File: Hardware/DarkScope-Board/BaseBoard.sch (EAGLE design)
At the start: 85 parts, among them IC1 7805DT, IC2 REG1117, IC3 7905, J1 DCJ0202, Q1 8MHz, T2 9014, U1 STM32F103CBT6, X1 TSW-102-07-G-S, X2 TSW-102-07-G-S, X3 MINI-USB-32005-301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

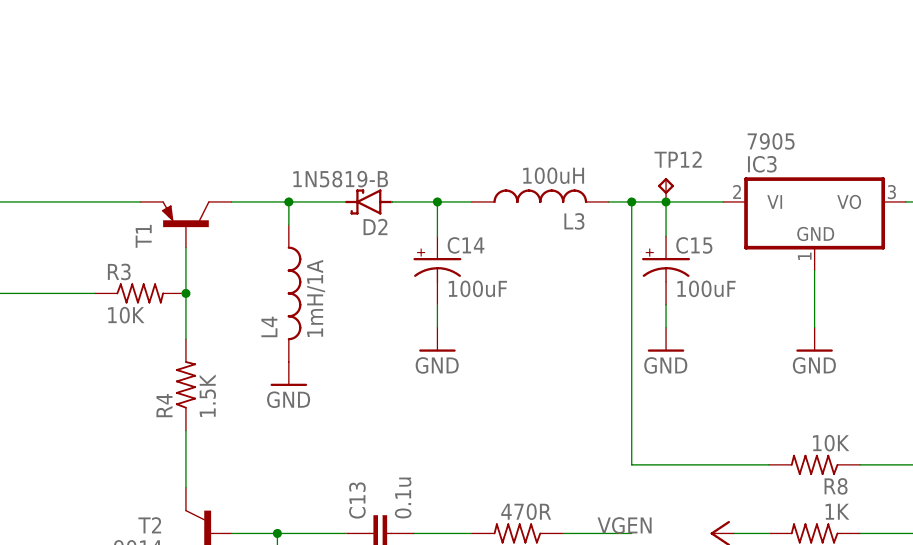
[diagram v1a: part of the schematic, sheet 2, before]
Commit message: Fixed BaseBoard Bugs
1. Ground Plane Not connected Properly
2. C14,C15 Reversed.
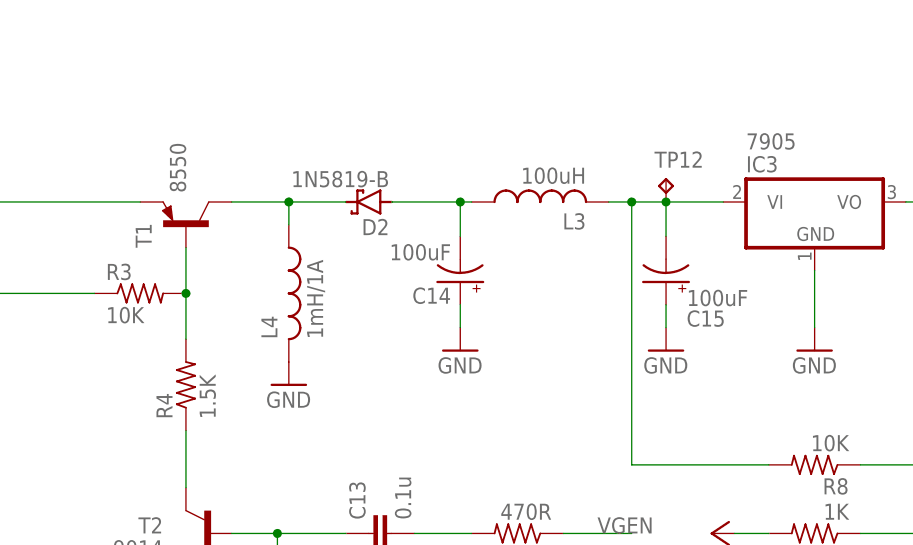
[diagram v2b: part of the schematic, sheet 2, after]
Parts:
- T1: value (none) -> 8550
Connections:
- net GND: now also C14.+, C15.+; no longer C14.-, C15.-
- net N$12: now also C14.-; no longer C14.+
- net N$13: now also C15.-; no longer C15.+
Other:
- moved on the sheet: C14, C15
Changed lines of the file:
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@@
 <setting verticaltext="up"/>
 </settings>
-<grid distance="0.1" unitdist="inch" unit="inch" style="lines" multiple="1" display="no" altdistance="0.01" altunitdist="inch" altunit="inch"/>
+<grid distance="0.01" unitdist="inch" unit="inch" style="lines" multiple="1" display="no" altdistance="0.01" altunitdist="inch" altunit="inch"/>
 <layers>
 <layer number="1" name="Top" color="4" fill="1" visible="no" active="no"/>
@@
 <part name="P+2" library="supply1" library_urn="urn:adsk.eagle:library:371" deviceset="+12V" device=""/>
 <part name="P+3" library="supply1" library_urn="urn:adsk.eagle:library:371" deviceset="+12V" device=""/>
-<part name="T1" library="transistor" library_urn="urn:adsk.eagle:library:402" deviceset="*-PNP-" device="TO92" package3d_urn="urn:adsk.eagle:package:28523/2"/>
+<part name="T1" library="transistor" library_urn="urn:adsk.eagle:library:402" deviceset="*-PNP-" device="TO92" package3d_urn="urn:adsk.eagle:package:28523/2" value="8550"/>
 <part name="R3" library="rcl" library_urn="urn:adsk.eagle:library:334" deviceset="R-US_" device="R0805" package3d_urn="urn:adsk.eagle:package:23553/2" value="10K"/>
 <part name="R4" library="rcl" library_urn="urn:adsk.eagle:library:334" deviceset="R-US_" device="R0805" package3d_urn="urn:adsk.eagle:package:23553/2" value="1.5K"/>
@@
 <instance part="T1" gate="G$1" x="200.66" y="107.95" smashed="yes" rot="R90">
 <attribute name="NAME" x="196.85" y="105.41" size="1.778" layer="95" rot="R90"/>
-<attribute name="VALUE" x="195.58" y="97.79" size="1.778" layer="96" rot="R90"/>
+<attribute name="VALUE" x="200.66" y="111.506" size="1.778" layer="96" rot="R90"/>
 </instance>
 <instance part="R3" gate="G$1" x="195.58" y="100.33" smashed="yes">
@@
 <attribute name="VALUE" x="223.266" y="113.919" size="1.778" layer="96" rot="R180"/>
 </instance>
-<instance part="C14" gate="G$1" x="228.6" y="104.14" smashed="yes">
-<attribute name="NAME" x="229.616" y="104.775" size="1.778" layer="95"/>
-<attribute name="VALUE" x="229.616" y="99.949" size="1.778" layer="96"/>
-</instance>
-<instance part="C15" gate="G$1" x="254" y="104.14" smashed="yes">
-<attribute name="NAME" x="255.016" y="104.775" size="1.778" layer="95"/>
-<attribute name="VALUE" x="255.016" y="99.949" size="1.778" layer="96"/>
-</instance>
-<instance part="GND20" gate="1" x="228.6" y="93.98" smashed="yes">
-<attribute name="VALUE" x="226.06" y="91.44" size="1.778" layer="96"/>
+<instance part="C14" gate="G$1" x="231.14" y="101.6" smashed="yes" rot="R180">
+<attribute name="NAME" x="230.124" y="100.965" size="1.778" layer="95" rot="R180"/>
+<attribute name="VALUE" x="230.124" y="105.791" size="1.778" layer="96" rot="R180"/>
+</instance>
+<instance part="C15" gate="G$1" x="254" y="101.6" smashed="yes" rot="R180">
+<attribute name="NAME" x="260.604" y="98.425" size="1.778" layer="95" rot="R180"/>
+<attribute name="VALUE" x="263.144" y="100.711" size="1.778" layer="96" rot="R180"/>
+</instance>
+<instance part="GND20" gate="1" x="231.14" y="93.98" smashed="yes">
+<attribute name="VALUE" x="228.6" y="91.44" size="1.778" layer="96"/>
 </instance>
 <instance part="GND21" gate="1" x="254" y="93.98" smashed="yes">
@@
 </segment>
 <segment>
-<pinref part="GND20" gate="1" pin="GND"/>
-<pinref part="C14" gate="G$1" pin="-"/>
-<wire x1="228.6" y1="96.52" x2="228.6" y2="99.06" width="0.1524" layer="91"/>
-</segment>
-<segment>
-<pinref part="GND21" gate="1" pin="GND"/>
-<pinref part="C15" gate="G$1" pin="-"/>
-<wire x1="254" y1="96.52" x2="254" y2="99.06" width="0.1524" layer="91"/>
-</segment>
-<segment>
 <pinref part="GND22" gate="1" pin="GND"/>
 <pinref part="IC3" gate="A1" pin="GND"/>
@@
 <pinref part="GND25" gate="1" pin="GND"/>
 <pinref part="TP15" gate="G$1" pin="TP"/>
+</segment>
+<segment>
+<pinref part="C15" gate="G$1" pin="+"/>
+<pinref part="GND21" gate="1" pin="GND"/>
+<wire x1="254" y1="99.06" x2="254" y2="96.52" width="0.1524" layer="91"/>
+</segment>
+<segment>
+<pinref part="C14" gate="G$1" pin="+"/>
+<pinref part="GND20" gate="1" pin="GND"/>
+<wire x1="231.14" y1="99.06" x2="231.14" y2="96.52" width="0.1524" layer="91"/>
 </segment>
 </net>
@@
 <pinref part="D2" gate="G$1" pin="A"/>
 <pinref part="L3" gate="G$1" pin="1"/>
-<wire x1="223.52" y1="110.49" x2="228.6" y2="110.49" width="0.1524" layer="91"/>
-<pinref part="C14" gate="G$1" pin="+"/>
-<wire x1="228.6" y1="110.49" x2="232.41" y2="110.49" width="0.1524" layer="91"/>
-<wire x1="228.6" y1="106.68" x2="228.6" y2="110.49" width="0.1524" layer="91"/>
-<junction x="228.6" y="110.49"/>
+<wire x1="223.52" y1="110.49" x2="231.14" y2="110.49" width="0.1524" layer="91"/>
+<pinref part="C14" gate="G$1" pin="-"/>
+<wire x1="231.14" y1="110.49" x2="232.41" y2="110.49" width="0.1524" layer="91"/>
+<wire x1="231.14" y1="106.68" x2="231.14" y2="110.49" width="0.1524" layer="91"/>
+<junction x="231.14" y="110.49"/>
 </segment>
 </net>
@@
 <pinref part="IC3" gate="A1" pin="VI"/>
 <wire x1="247.65" y1="110.49" x2="250.19" y2="110.49" width="0.1524" layer="91"/>
-<pinref part="C15" gate="G$1" pin="+"/>
 <wire x1="250.19" y1="110.49" x2="254" y2="110.49" width="0.1524" layer="91"/>
 <wire x1="254" y1="110.49" x2="260.35" y2="110.49" width="0.1524" layer="91"/>
-<wire x1="254" y1="106.68" x2="254" y2="110.49" width="0.1524" layer="91"/>
 <junction x="254" y="110.49"/>
 <pinref part="TP12" gate="G$1" pin="TP"/>
@@
 <wire x1="250.19" y1="81.28" x2="265.43" y2="81.28" width="0.1524" layer="91"/>
 <junction x="250.19" y="110.49"/>
-</segment>
-</net>
+<pinref part="C15" gate="G$1" pin="-"/>
+<wire x1="254" y1="106.68" x2="254" y2="110.49" width="0.1524" layer="91"/>
+</segment>
+</net>

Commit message: Updated BaseBoard as per DFM Request
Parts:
- JMP1, JMP2, JMP3: value 0R-JUMPC -> 0R-JUMPA; device jump-0r-smd:0R-JUMPC -> jump-0r-smd:0R-JUMPA
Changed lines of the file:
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@@
 <setting verticaltext="up"/>
 </settings>
-<grid distance="0.01" unitdist="inch" unit="inch" style="lines" multiple="1" display="no" altdistance="0.01" altunitdist="inch" altunit="inch"/>
+<grid distance="0.1" unitdist="inch" unit="inch" style="lines" multiple="1" display="no" altdistance="0.01" altunitdist="inch" altunit="inch"/>
 <layers>
 <layer number="1" name="Top" color="4" fill="1" visible="no" active="no"/>
@@
 <part name="GND13" library="supply1" library_urn="urn:adsk.eagle:library:371" deviceset="GND" device=""/>
 <part name="P+1" library="supply1" library_urn="urn:adsk.eagle:library:371" deviceset="+5V" device=""/>
-<part name="JMP1" library="jump-0r-smd" library_urn="urn:adsk.eagle:library:251" deviceset="0R-JUMP" device="C" package3d_urn="urn:adsk.eagle:package:15386/1"/>
+<part name="JMP1" library="jump-0r-smd" library_urn="urn:adsk.eagle:library:251" deviceset="0R-JUMP" device="A" package3d_urn="urn:adsk.eagle:package:15385/1" value="0R-JUMPA"/>
 <part name="GND14" library="supply1" library_urn="urn:adsk.eagle:library:371" deviceset="GND" device=""/>
-<part name="JMP2" library="jump-0r-smd" library_urn="urn:adsk.eagle:library:251" deviceset="0R-JUMP" device="C" package3d_urn="urn:adsk.eagle:package:15386/1"/>
+<part name="JMP2" library="jump-0r-smd" library_urn="urn:adsk.eagle:library:251" deviceset="0R-JUMP" device="A" package3d_urn="urn:adsk.eagle:package:15385/1" value="0R-JUMPA"/>
 <part name="TP7" library="testpad" library_urn="urn:adsk.eagle:library:385" deviceset="TP" device="B1,27" package3d_urn="urn:adsk.eagle:package:27944/2"/>
 <part name="TP8" library="testpad" library_urn="urn:adsk.eagle:library:385" deviceset="TP" device="B1,27" package3d_urn="urn:adsk.eagle:package:27944/2"/>
@@
 <part name="R9" library="rcl" library_urn="urn:adsk.eagle:library:334" deviceset="R-US_" device="R0805" package3d_urn="urn:adsk.eagle:package:23553/2" value="180E"/>
 <part name="P+4" library="supply1" library_urn="urn:adsk.eagle:library:371" deviceset="+5V" device=""/>
-<part name="JMP3" library="jump-0r-smd" library_urn="urn:adsk.eagle:library:251" deviceset="0R-JUMP" device="C" package3d_urn="urn:adsk.eagle:package:15386/1"/>
+<part name="JMP3" library="jump-0r-smd" library_urn="urn:adsk.eagle:library:251" deviceset="0R-JUMP" device="A" package3d_urn="urn:adsk.eagle:package:15385/1" value="0R-JUMPA"/>
 <part name="P+5" library="supply1" library_urn="urn:adsk.eagle:library:371" deviceset="+12V" device=""/>
 <part name="GND29" library="supply1" library_urn="urn:adsk.eagle:library:371" deviceset="GND" device=""/>
